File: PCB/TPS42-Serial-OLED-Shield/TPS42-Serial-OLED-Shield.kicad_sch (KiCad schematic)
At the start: 13 parts, among them J4 PJ-320A, J5 Conn_01x06, J6 OLED

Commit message: renaming
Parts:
- J4: footprint TPS42-Shield:MJ-4PP-9-reversable -> TPS42-Serial-OLED-Shield:MJ-4PP-9-reversable
- J6: footprint TPS42-Shield:OLED -> TPS42-Serial-OLED-Shield:OLED
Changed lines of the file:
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@@
       (effects (font (size 1.27 1.27)) (justify left))
     )
-    (property "Footprint" "TPS42-Shield:OLED" (id 2) (at 26.924 39.116 0)
+    (property "Footprint" "TPS42-Serial-OLED-Shield:OLED" (id 2) (at 26.924 39.116 0)
       (effects (font (size 1.27 1.27)) hide)
     )
@@
     (property "Reference" "J4" (id 0) (at 31.877 76.0772 0))
     (property "Value" "PJ-320A" (id 1) (at 32.893 61.0785 0))
-    (property "Footprint" "TPS42-Shield:MJ-4PP-9-reversable" (id 2) (at 33.02 68.834 0)
+    (property "Footprint" "TPS42-Serial-OLED-Shield:MJ-4PP-9-reversable" (id 2) (at 33.02 68.834 0)
       (effects (font (size 1.27 1.27)) hide)
     )
@@
     )
     (path "/bb29eadf-6880-457d-8855-ab29e518b76b"
-      (reference "J4") (unit 1) (value "PJ-320A") (footprint "TPS42-Shield:MJ-4PP-9-reversable")
+      (reference "J4") (unit 1) (value "PJ-320A") (footprint "TPS42-Serial-OLED-Shield:MJ-4PP-9-reversable")
     )
     (path "/fdb5a690-9a4d-42dd-a69c-992990219ba2"
@@
     )
     (path "/4d8eb33d-7456-4ffb-9897-c9d55e9b477e"
-      (reference "J6") (unit 1) (value "OLED") (footprint "TPS42-Shield:OLED")
+      (reference "J6") (unit 1) (value "OLED") (footprint "TPS42-Serial-OLED-Shield:OLED")
     )
     (path "/a0cc0da0-95a4-4b91-a824-b7e7df5c5bc5"

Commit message: finalizing
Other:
- title: (none) -> TPS42 OLED & TRRS Shield
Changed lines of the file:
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@@
 (kicad_sch (version 20211123) (generator eeschema)
   (paper "A4")
+  (title_block
+    (title "TPS42 OLED & TRRS Shield")
+    (date "2022-05-19")
+    (rev "${Revision}")
+  )
   (junction (at 40.64 51.308) (diameter 0) (color 0 0 0 0)
   )

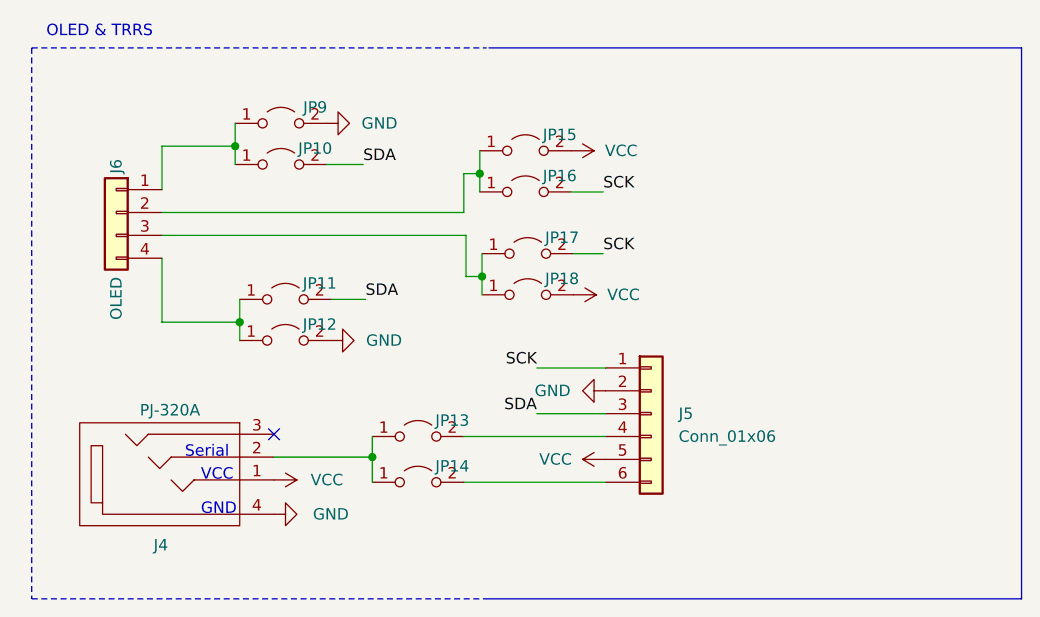
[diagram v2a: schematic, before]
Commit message: removed serial jumber
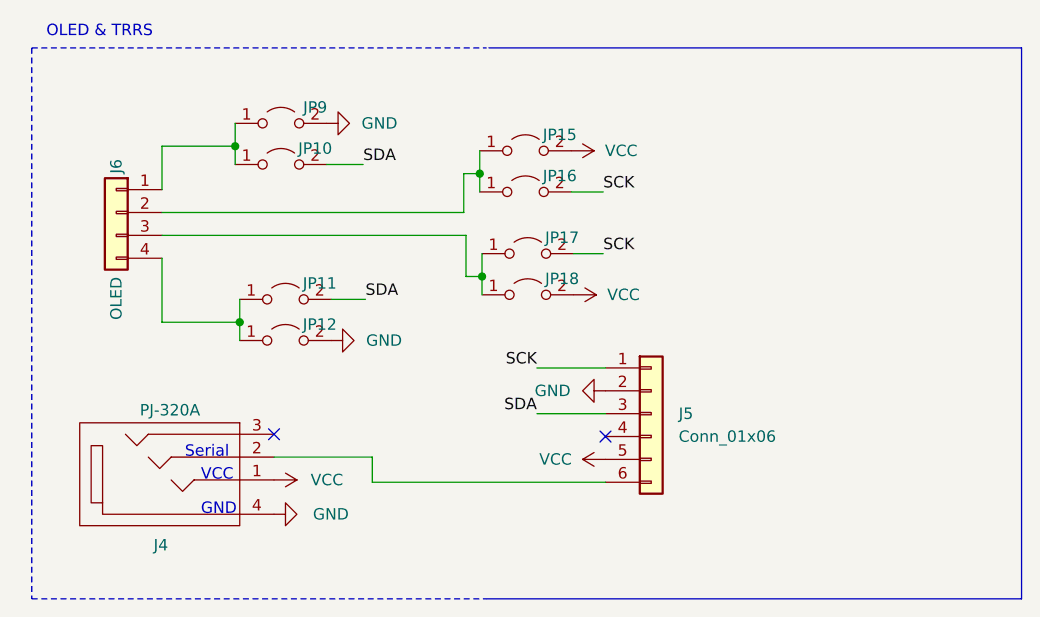
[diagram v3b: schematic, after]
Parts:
- removed JP13, JP14: Jumper_2_Open, Jumper:SolderJumper-2_P1.3mm_Open_TrianglePad1.0x1.5mm, symbol Jumper:Jumper_2_Open
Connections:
- net at J4.2: now also J5.6 (Pin_6)
- no-connect marks 1 -> 2
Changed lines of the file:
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@@
   (junction (at 67.564 46.228) (diameter 0) (color 0 0 0 0)
   )
-  (junction (at 55.372 66.294) (diameter 0) (color 0 0 0 0)
-  )
   (junction (at 40.132 31.75) (diameter 0) (color 0 0 0 0)
   )
   (no_connect (at 44.45 63.754))
+  (no_connect (at 81.28 64.008))
   (wire (pts (xy 73.66 56.388) (xy 81.28 56.388))
     (stroke (width 0) (type default) (color 0 0 0 0))
@@
     (stroke (width 0) (type default) (color 0 0 0 0))
   )
-  (wire (pts (xy 55.372 64.008) (xy 55.372 66.294))
-    (stroke (width 0) (type default) (color 0 0 0 0))
-  )
   (wire (pts (xy 65.532 39.116) (xy 65.532 34.798))
     (stroke (width 0) (type default) (color 0 0 0 0))
@@
     (stroke (width 0) (type default) (color 0 0 0 0))
   )
-  (wire (pts (xy 65.532 64.008) (xy 81.28 64.008))
-    (stroke (width 0) (type default) (color 0 0 0 0))
-  )
   (wire (pts (xy 40.132 31.75) (xy 40.132 33.782))
     (stroke (width 0) (type default) (color 0 0 0 0))
@@
     (stroke (width 0) (type default) (color 0 0 0 0))
   )
+  (wire (pts (xy 55.372 69.088) (xy 81.28 69.088))
+    (stroke (width 0) (type default) (color 0 0 0 0))
+  )
   (wire (pts (xy 73.66 61.468) (xy 81.28 61.468))
     (stroke (width 0) (type default) (color 0 0 0 0))
@@
   )
   (wire (pts (xy 65.786 41.656) (xy 65.786 46.228))
-    (stroke (width 0) (type default) (color 0 0 0 0))
-  )
-  (wire (pts (xy 65.532 69.088) (xy 81.28 69.088))
     (stroke (width 0) (type default) (color 0 0 0 0))
   )
@@
     (pin "4")
   )
-  (symbol (lib_id "Jumper:Jumper_2_Open") (at 60.452 64.008 0) (unit 1)
-    (in_bom yes) (on_board yes)
-    (property "Reference" "JP13" (id 0) (at 64.262 62.23 0))
-    (property "Value" "Jumper_2_Open" (id 1) (at 60.452 59.436 0)
-      (effects (font (size 1.27 1.27)) hide)
-    )
-    (property "Footprint" "Jumper:SolderJumper-2_P1.3mm_Open_TrianglePad1.0x1.5mm" (id 2) (at 60.452 64.008 0)
-      (effects (font (size 1.27 1.27)) hide)
-    )
-    (property "Datasheet" "~" (id 3) (at 60.452 64.008 0)
-      (effects (font (size 1.27 1.27)) hide)
-    )
-    (pin "1")
-    (pin "2")
-  )
   (symbol (lib_id "power:GND") (at 50.8 53.34 90) (unit 1)
     (in_bom yes) (on_board yes)
@@
     )
     (pin "1")
-  )
-  (symbol (lib_id "Jumper:Jumper_2_Open") (at 60.452 69.088 0) (unit 1)
-    (in_bom yes) (on_board yes)
-    (property "Reference" "JP14" (id 0) (at 64.262 67.31 0))
-    (property "Value" "Jumper_2_Open" (id 1) (at 60.452 64.516 0)
-      (effects (font (size 1.27 1.27)) hide)
-    )
-    (property "Footprint" "Jumper:SolderJumper-2_P1.3mm_Open_TrianglePad1.0x1.5mm" (id 2) (at 60.452 69.088 0)
-      (effects (font (size 1.27 1.27)) hide)
-    )
-    (property "Datasheet" "~" (id 3) (at 60.452 69.088 0)
-      (effects (font (size 1.27 1.27)) hide)
-    )
-    (pin "1")
-    (pin "2")
   )
   (symbol (lib_id "Connector_Generic:Conn_01x06") (at 86.36 61.468 0) (unit 1)
@@
       (reference "JP12") (unit 1) (value "Jumper_2_Open") (footprint "Jumper:SolderJumper-2_P1.3mm_Open_TrianglePad1.0x1.5mm")
     )
-    (path "/bbb7e4aa-09d6-4fac-acd5-80e344333c9b"
-      (reference "JP13") (unit 1) (value "Jumper_2_Open") (footprint "Jumper:SolderJumper-2_P1.3mm_Open_TrianglePad1.0x1.5mm")
-    )
-    (path "/f1ba9cb7-8a35-4bff-8008-7beabc6af2dd"
-      (reference "JP14") (unit 1) (value "Jumper_2_Open") (footprint "Jumper:SolderJumper-2_P1.3mm_Open_TrianglePad1.0x1.5mm")
-    )
     (path "/6fe6a09d-14ea-40ef-8fb1-e53eb876af95"
